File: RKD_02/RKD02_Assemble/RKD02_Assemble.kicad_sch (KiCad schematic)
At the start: 162 parts, among them J1 Qwiic_RA, J2 Qwiic_RA, M1 Mark, M3 Mark, M4 Mark, M5 Mark, M6 Mark, SW1 SW_Push, SW10 SW_Push, SW11 SW_Push, SW12 SW_Push, SW13 SW_Push, SW14 SW_Push, SW15 SW_Push, SW16 SW_Push, SW17 SW_Push, SW18 SW_Push, SW19 SW_Push, SW2 SW_Push, SW20 SW_Push, SW21 SW_Push, SW22 SW_Push, SW23 SW_Push, SW24 SW_Push, SW25 SW_Push, SW26 SW_Push, SW27 SW_Push, SW28 SW_Push, SW29 SW_Push, SW3 SW_Push, SW30 SW_Push, SW31 SW_Push, SW32 SW_Push, SW33 SW_Push, SW34 SW_Push, SW35 SW_Push, SW36 RotaryEncoder_Switch, SW4 SW_Push, SW40 RotaryEncoder_Switch, SW5 SW_Push, SW51 SW_Push, SW52 SW_Push, SW53 SW_Push, SW54 SW_Push, SW55 SW_Push, SW56 SW_Push, SW57 SW_Push, SW58 SW_Push, SW59 SW_Push, SW6 SW_Push, SW60 SW_Push, SW61 SW_Push, SW62 SW_Push, SW63 SW_Push, SW64 SW_Push, SW65 SW_Push, SW66 SW_Push, SW67 SW_Push, SW68 SW_Push, SW69 SW_Push, SW7 SW_Push, SW70 SW_Push, SW71 SW_Push, SW72 SW_Push, SW73 SW_Push, SW74 SW_Push, SW75 SW_Push, SW76 SW_Push, SW77 SW_Push, SW78 SW_Push, SW79 SW_Push, SW8 SW_Push, SW80 SW_Push, SW81 SW_Push, SW82 SW_Push, SW83 SW_Push, SW84 SW_Push, SW85 SW_Push, SW86 SW_Push, SW87 SW_Push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

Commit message: RKD02 Revision
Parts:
- added M7: Mark, kbd_Hole:m2_Spacer_Hole_hex, symbol BrownSugar_KBD:Mark
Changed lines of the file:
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@@
+	)
+	(symbol
+		(lib_id "BrownSugar_KBD:Mark")
+		(at 391.16 31.75 0)
+		(unit 1)
+		(exclude_from_sim no)
+		(in_bom yes)
+		(on_board yes)
+		(dnp no)
+		(fields_autoplaced yes)
+		(property "Reference" "M7"
+			(at 393.7 30.4799 0)
+			(effects
+				(font
+					(size 1.27 1.27)
+				)
+				(justify left)
+			)
+		)
+		(property "Value" "Mark"
+			(at 393.7 33.0199 0)
+			(effects
+				(font
+					(size 1.27 1.27)
+				)
+				(justify left)
+			)
+		)
+		(property "Footprint" "kbd_Hole:m2_Spacer_Hole_hex"
+			(at 391.16 31.75 0)
+			(effects
+				(font
+					(size 1.27 1.27)
+				)
+				(hide yes)
+			)
+		)
+		(property "Datasheet" ""
+			(at 391.16 31.75 0)
+			(effects
+				(font
+					(size 1.27 1.27)
+				)
+				(hide yes)
+			)
+		)
+		(property "Description" ""
+			(at 391.16 31.75 0)
+			(effects
+				(font
+					(size 1.27 1.27)
+				)
+				(hide yes)
+			)
+		)
+		(instances
+			(project "RKD02_Assemble"
+				(path "/01a859e0-5a12-4534-b9e3-6128f69eb8fc"
+					(reference "M7")
+					(unit 1)
+				)
+			)
+		)
 	)
 	(symbol

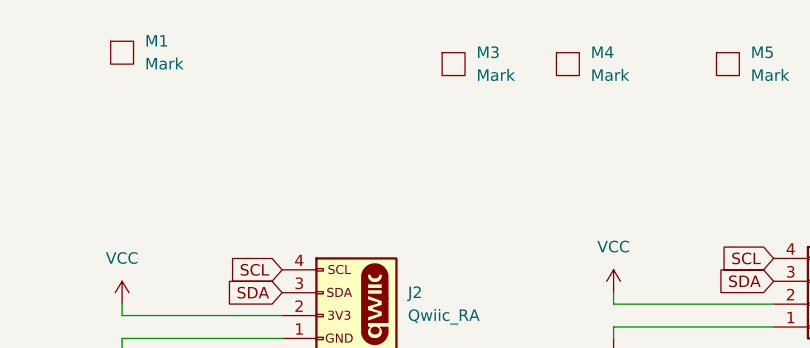
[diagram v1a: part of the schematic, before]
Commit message: RKD02_AddScrewHoles
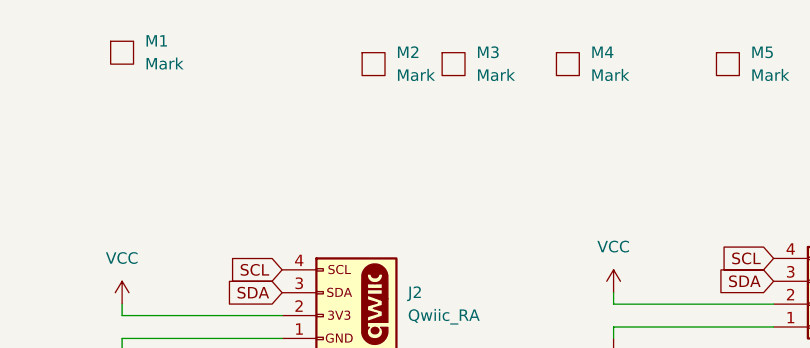
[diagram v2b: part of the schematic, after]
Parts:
- added M2: Mark, kbd_Hole:m2_Spacer_Hole_hex, symbol BrownSugar_KBD:Mark
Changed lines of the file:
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@@
+	)
+	(symbol
+		(lib_id "BrownSugar_KBD:Mark")
+		(at 337.82 22.86 0)
+		(unit 1)
+		(exclude_from_sim no)
+		(in_bom yes)
+		(on_board yes)
+		(dnp no)
+		(fields_autoplaced yes)
+		(property "Reference" "M2"
+			(at 340.36 21.5899 0)
+			(effects
+				(font
+					(size 1.27 1.27)
+				)
+				(justify left)
+			)
+		)
+		(property "Value" "Mark"
+			(at 340.36 24.1299 0)
+			(effects
+				(font
+					(size 1.27 1.27)
+				)
+				(justify left)
+			)
+		)
+		(property "Footprint" "kbd_Hole:m2_Spacer_Hole_hex"
+			(at 337.82 22.86 0)
+			(effects
+				(font
+					(size 1.27 1.27)
+				)
+				(hide yes)
+			)
+		)
+		(property "Datasheet" ""
+			(at 337.82 22.86 0)
+			(effects
+				(font
+					(size 1.27 1.27)
+				)
+				(hide yes)
+			)
+		)
+		(property "Description" ""
+			(at 337.82 22.86 0)
+			(effects
+				(font
+					(size 1.27 1.27)
+				)
+				(hide yes)
+			)
+		)
+		(instances
+			(project "RKD02_Assemble"
+				(path "/01a859e0-5a12-4534-b9e3-6128f69eb8fc"
+					(reference "M2")
+					(unit 1)
+				)
+			)
+		)
 	)
 	(symbol

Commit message: RKD02 大量に調整
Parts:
- removed SW36: RotaryEncoder_Switch, BrownSugar_KBD:RotaryEncoder_EC11-Switch, symbol Device:RotaryEncoder_Switch
- SW31: footprint BrownSugar_KBD:SW_PUSH_6x3mm -> Rikkodo_FootPrint:rkd_Asm_ChocV1V2_Hotswap_1u
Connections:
- net RE2_A is gone; now on net RE1_A: SW40.A, U1.22 (GPIO17)
- net RE2_B is gone; now on net RE1_B: SW40.B, U1.16 (GPIO12)
- net RE1_A: no longer U1.1 (GPIO0)
- net RE1_B: no longer U1.2 (GPIO1)
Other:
- moved on the sheet: D31, SW31

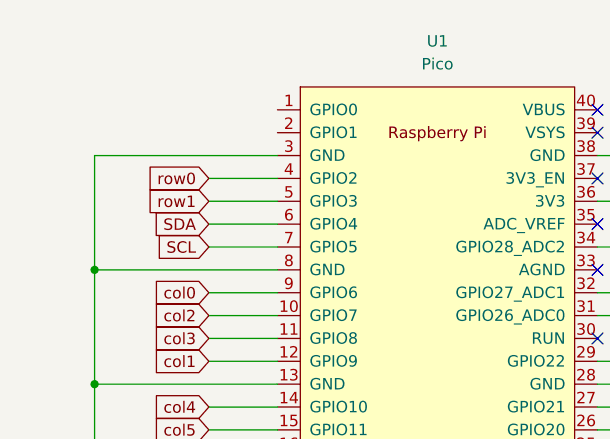
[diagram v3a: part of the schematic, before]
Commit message: RKD02 結線を変更
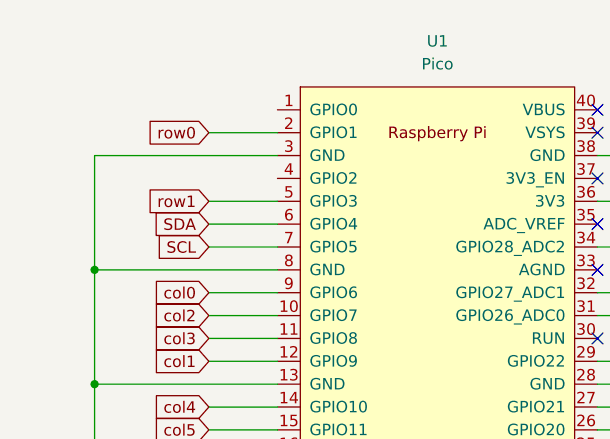
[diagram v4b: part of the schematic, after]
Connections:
- net row0: now also U1.2 (GPIO1); no longer U1.4 (GPIO2)
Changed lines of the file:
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@@
+	(wire
+		(pts
+			(xy 38.1 30.48) (xy 45.72 30.48)
+		)
+		(stroke
+			(width 0)
+			(type default)
+		)
+	)
 	(wire
 		(pts
@@
 	(wire
 		(pts
-			(xy 38.1 35.56) (xy 45.72 35.56)
-		)
-		(stroke
-			(width 0)
-			(type default)
-		)
-	)
-	(wire
-		(pts
 			(xy 199.39 185.42) (xy 220.98 185.42)
 		)
@@
 		)
 	)
+	(global_label "row0"
+		(shape input)
+		(at 38.1 30.48 180)
+		(fields_autoplaced yes)
+		(effects
+			(font
+				(size 1.27 1.27)
+			)
+			(justify right)
+		)
+		(property "Intersheetrefs" "${INTERSHEET_REFS}"
+			(at 30.6396 30.48 0)
+			(effects
+				(font
+					(size 1.27 1.27)
+				)
+				(justify right)
+				(hide yes)
+			)
+		)
+	)
 	(global_label "col8"
 		(shape input)
@@
 				(hide yes)
 			)
-		)
-	)
-	(global_label "row0"
-		(shape input)
-		(at 38.1 35.56 180)
-		(fields_autoplaced yes)
-		(effects
-			(font
-				(size 1.27 1.27)
-			)
-			(justify right)
-		)
-		(property "Intersheetrefs" "${INTERSHEET_REFS}"
-			(at 30.6396 35.56 0)
-			(effects
-				(font
-					(size 1.27 1.27)
-				)
-				(justify right)
-				(hide yes)
-			)

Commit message: RKD02 _I2CコネクタをSPI使える組み合わせに変更
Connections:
- net col0: now also U1.6 (GPIO4); no longer U1.9 (GPIO6)
- net col2: now also U1.7 (GPIO5); no longer U1.10 (GPIO7)
- net row0: now also U1.1 (GPIO0); no longer U1.2 (GPIO1)
- net row1: now also U1.2 (GPIO1); no longer U1.5 (GPIO3)
- net SCL renamed SCL-DIO
- net SCL-DIO: now also U1.10 (GPIO7); no longer U1.7 (GPIO5)
- net SDA renamed SDA-SCK
- net SDA-SCK: now also U1.9 (GPIO6); no longer U1.6 (GPIO4)

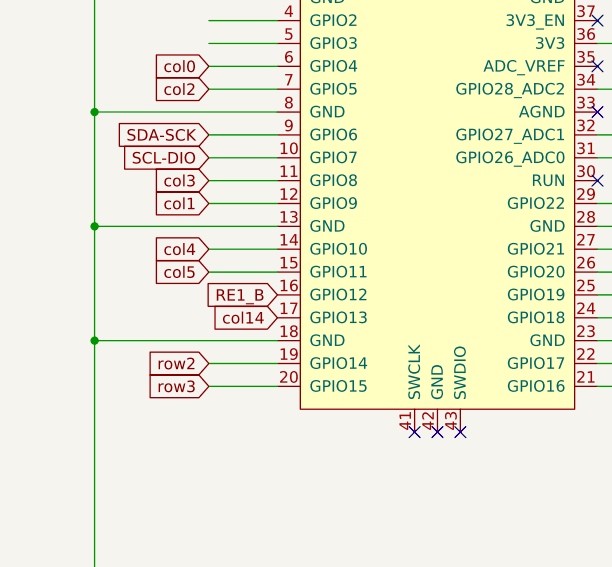
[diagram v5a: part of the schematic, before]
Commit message: RKD02_コネクタ配置を変更
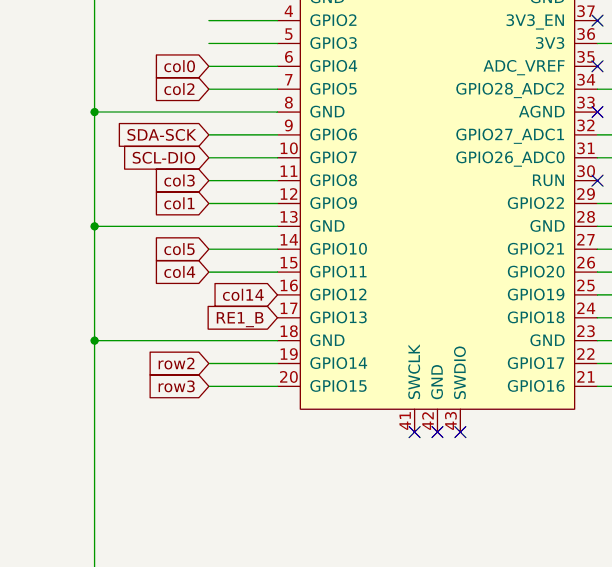
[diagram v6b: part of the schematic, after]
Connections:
- net RE1_B: now also U1.17 (GPIO13); no longer U1.16 (GPIO12)
- net col14: now also U1.16 (GPIO12); no longer U1.17 (GPIO13)
- net col4: now also U1.15 (GPIO11); no longer U1.14 (GPIO10)
- net col5: now also U1.14 (GPIO10); no longer U1.15 (GPIO11)

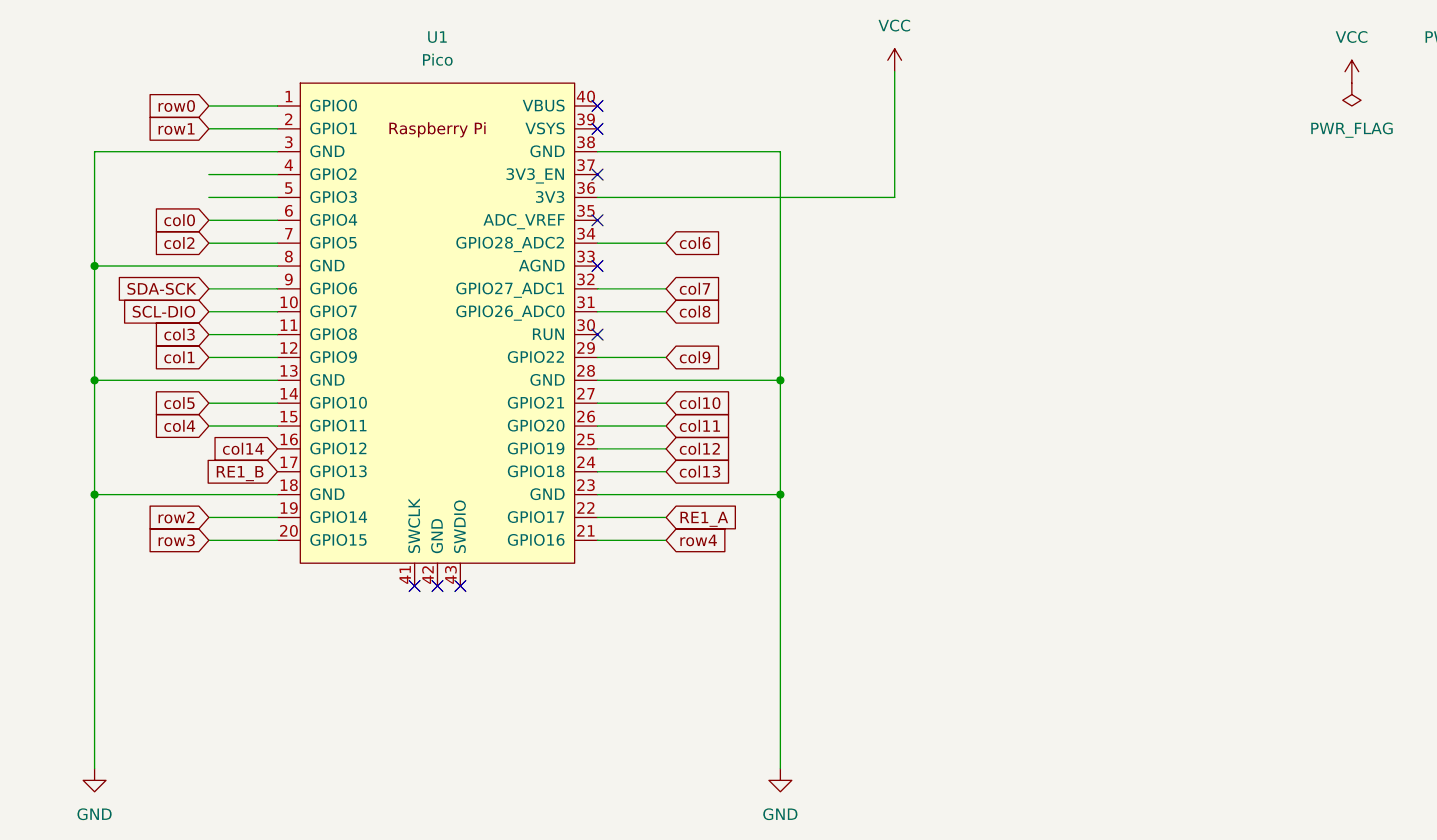
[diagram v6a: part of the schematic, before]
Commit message: RKD02 6Pin追加
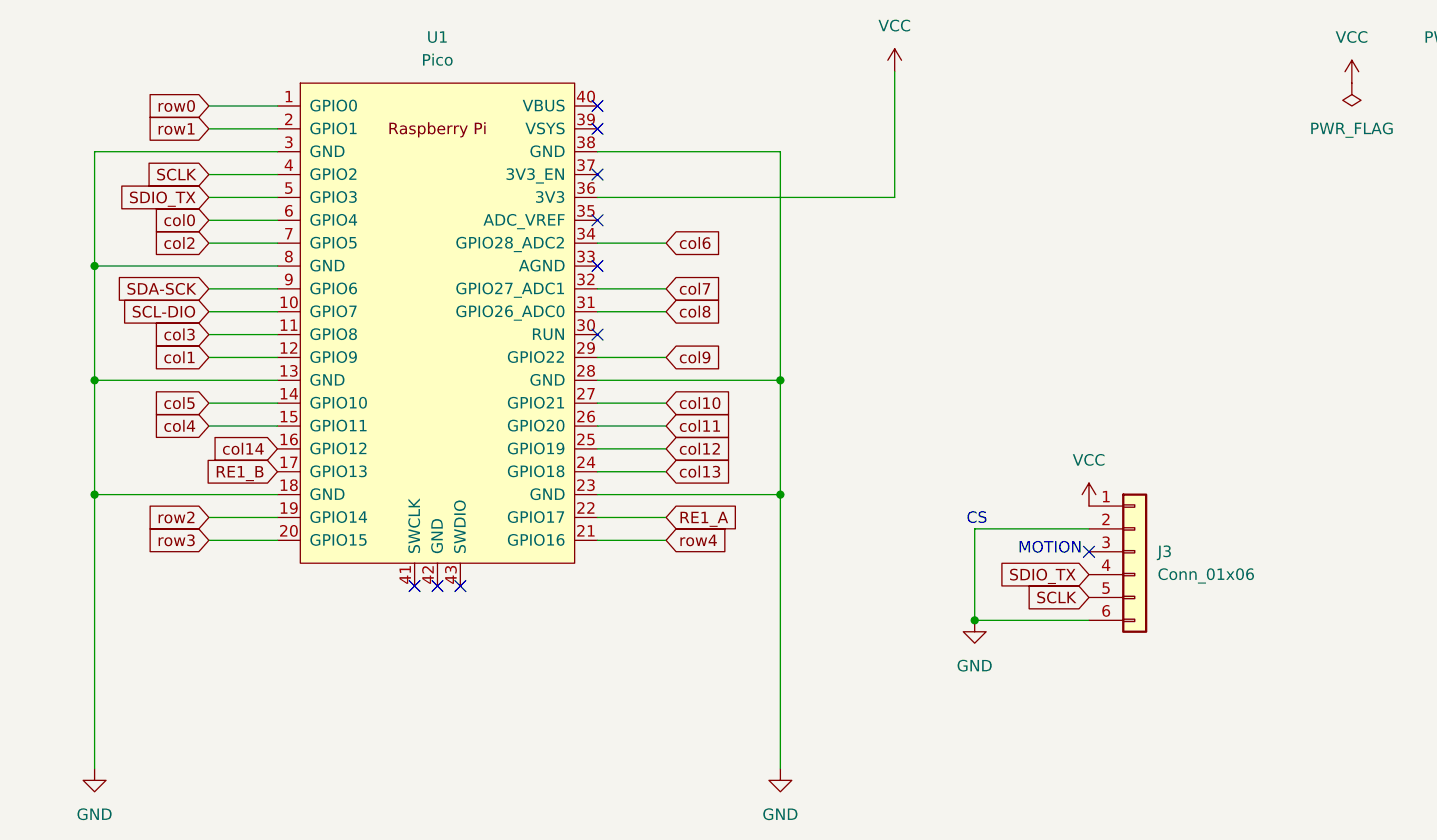
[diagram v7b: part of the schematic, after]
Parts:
- added J3: Conn_01x06, Connector_FFC-FPC:Hirose_FH12-6S-0.5SH_1x06-1MP_P0.50mm_Horizontal, symbol Connector_Generic:Conn_01x06
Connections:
- net GND: now also J3.2 (Pin_2), J3.6 (Pin_6)
- net VCC: now also J3.1 (Pin_1)
- net SCLK: now reaches U1.4 (GPIO2)
- net SCLK: now also J3.5 (Pin_5)
- net SDIO_TX: now reaches U1.5 (GPIO3)
- net SDIO_TX: now also J3.4 (Pin_4)
- no-connect marks 9 -> 10
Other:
- note added: "CS"
- note added: "MOTION"

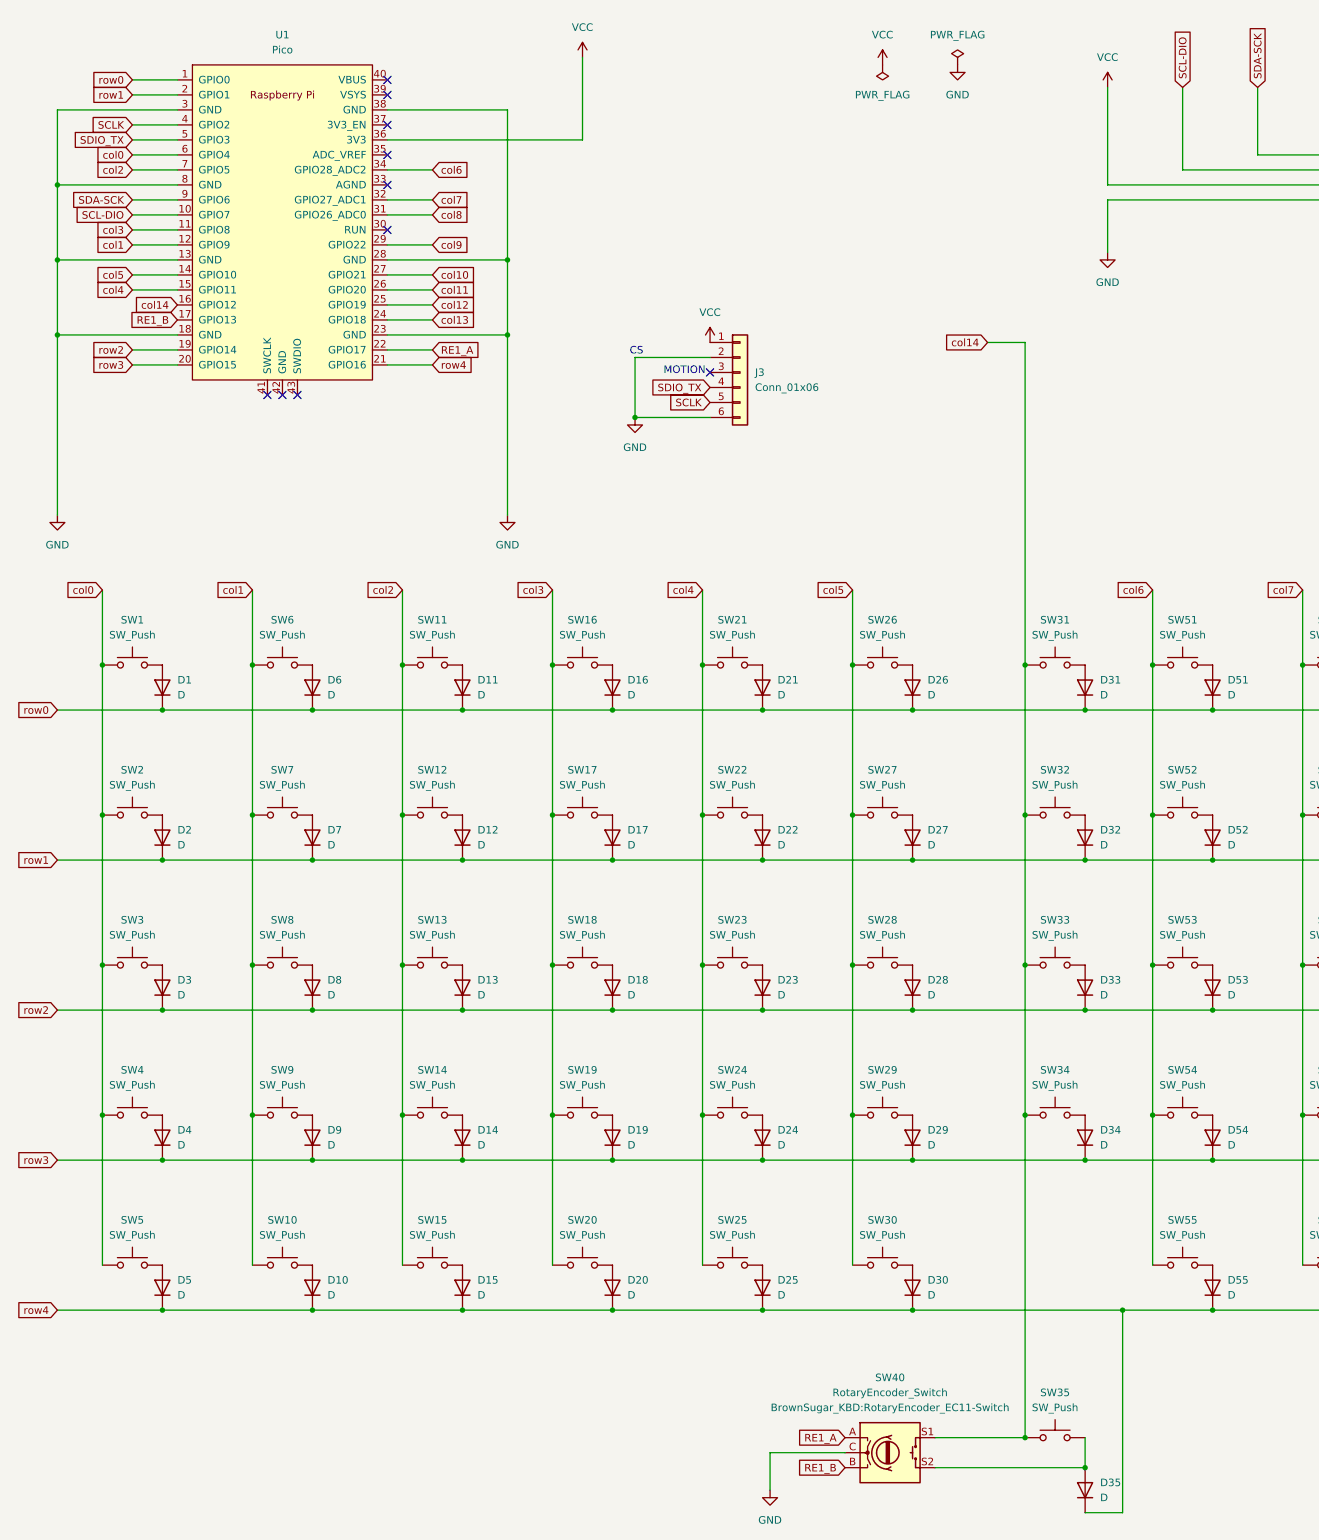
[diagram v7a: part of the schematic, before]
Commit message: RKD02 不要なCOL14を削除
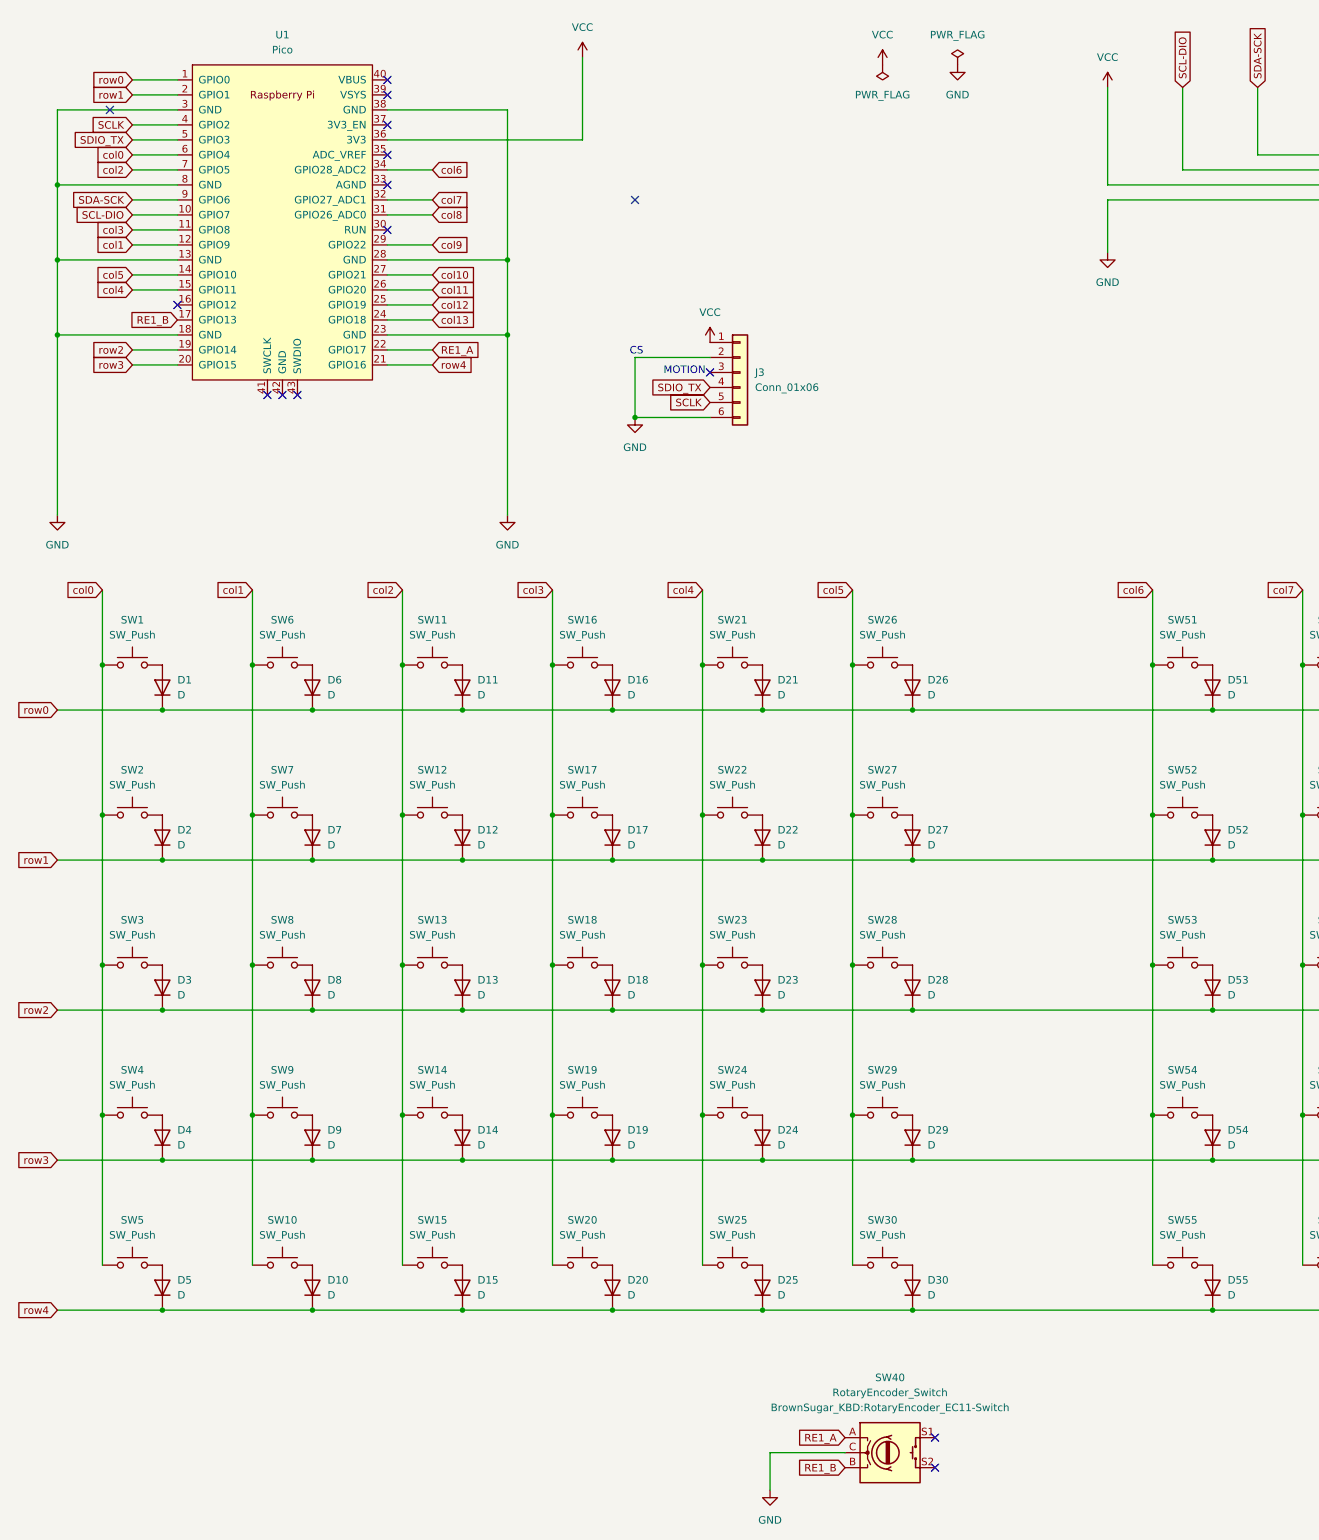
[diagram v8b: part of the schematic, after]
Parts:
- removed D31, D32, D33, D34, D35: D, kbd_Parts:Diode_SMD, symbol Device:D
- removed SW31: SW_Push, Rikkodo_FootPrint:rkd_Asm_ChocV1V2_Hotswap_1u, symbol Switch:SW_Push
- removed SW32, SW33, SW34, SW35: SW_Push, BrownSugar_KBD:SW_PUSH_6x3mm, symbol Switch:SW_Push
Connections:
- net col14: no longer names the net of U1.16 (GPIO12)
- net col14: no longer SW40.S1
- no-connect marks 10 -> 15
